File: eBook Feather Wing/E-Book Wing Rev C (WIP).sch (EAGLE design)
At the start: 96 parts, among them IC1 MCP23008/SO, IC2 23K256-I/SN, J1 MJ-3502N, Q1 IRLML0100, SW1 SPDT_SWITCH

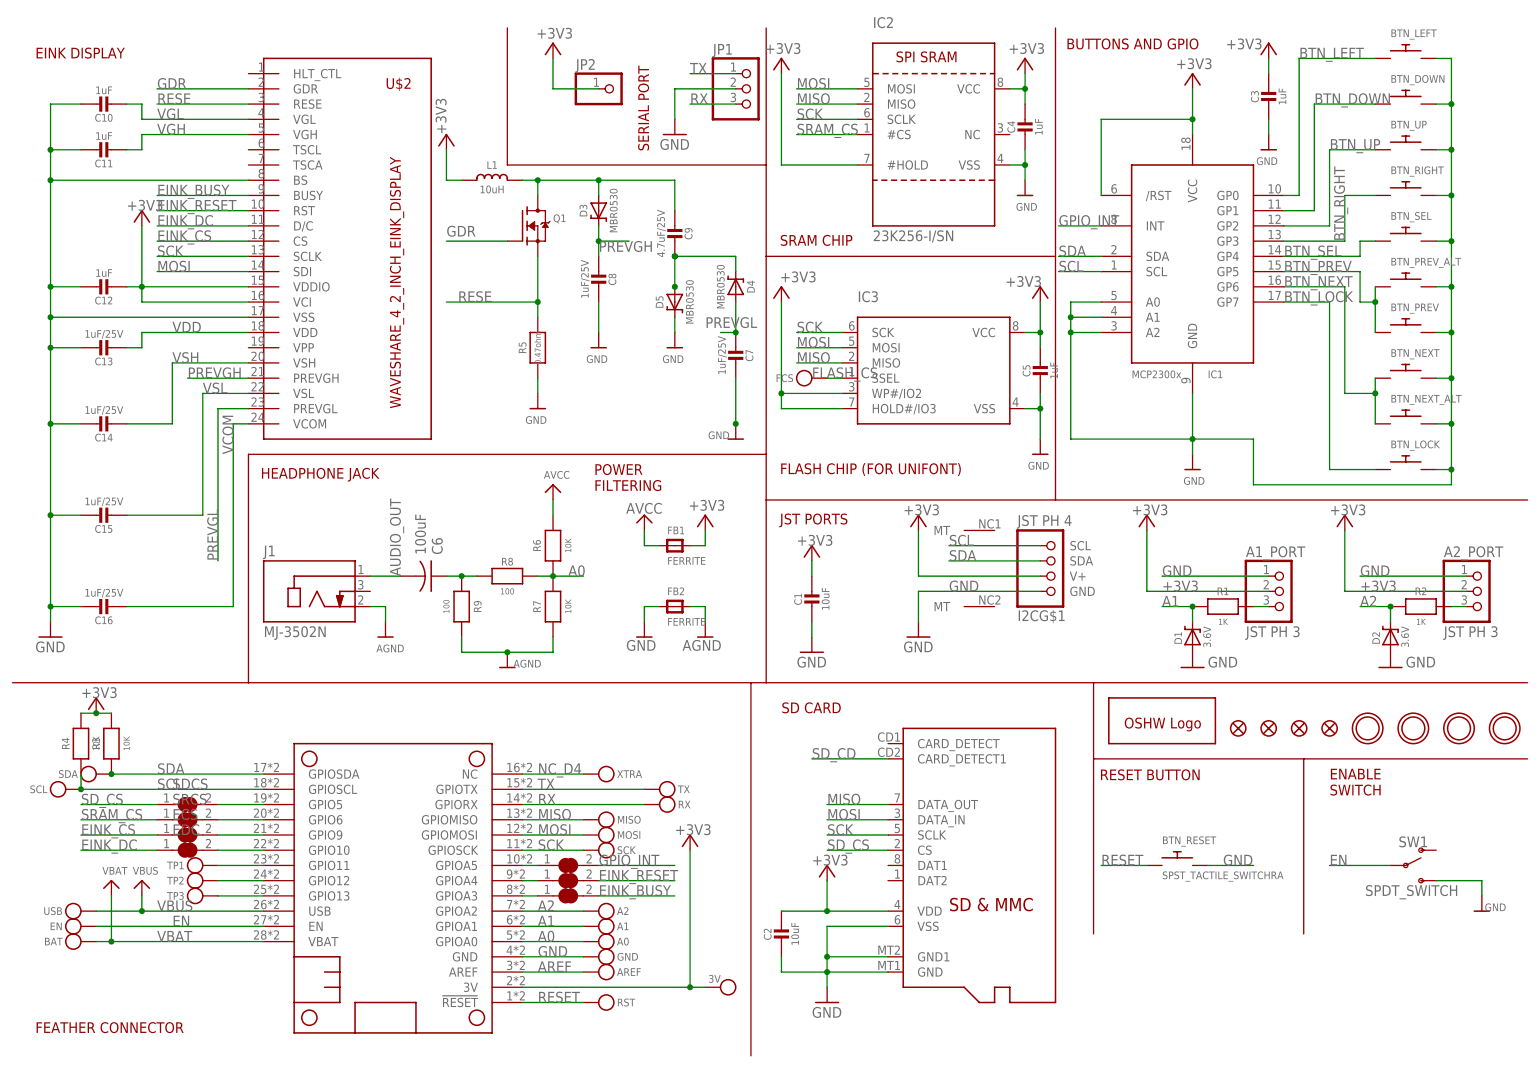
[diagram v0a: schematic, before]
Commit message: surface mount part swap, two more fiducials
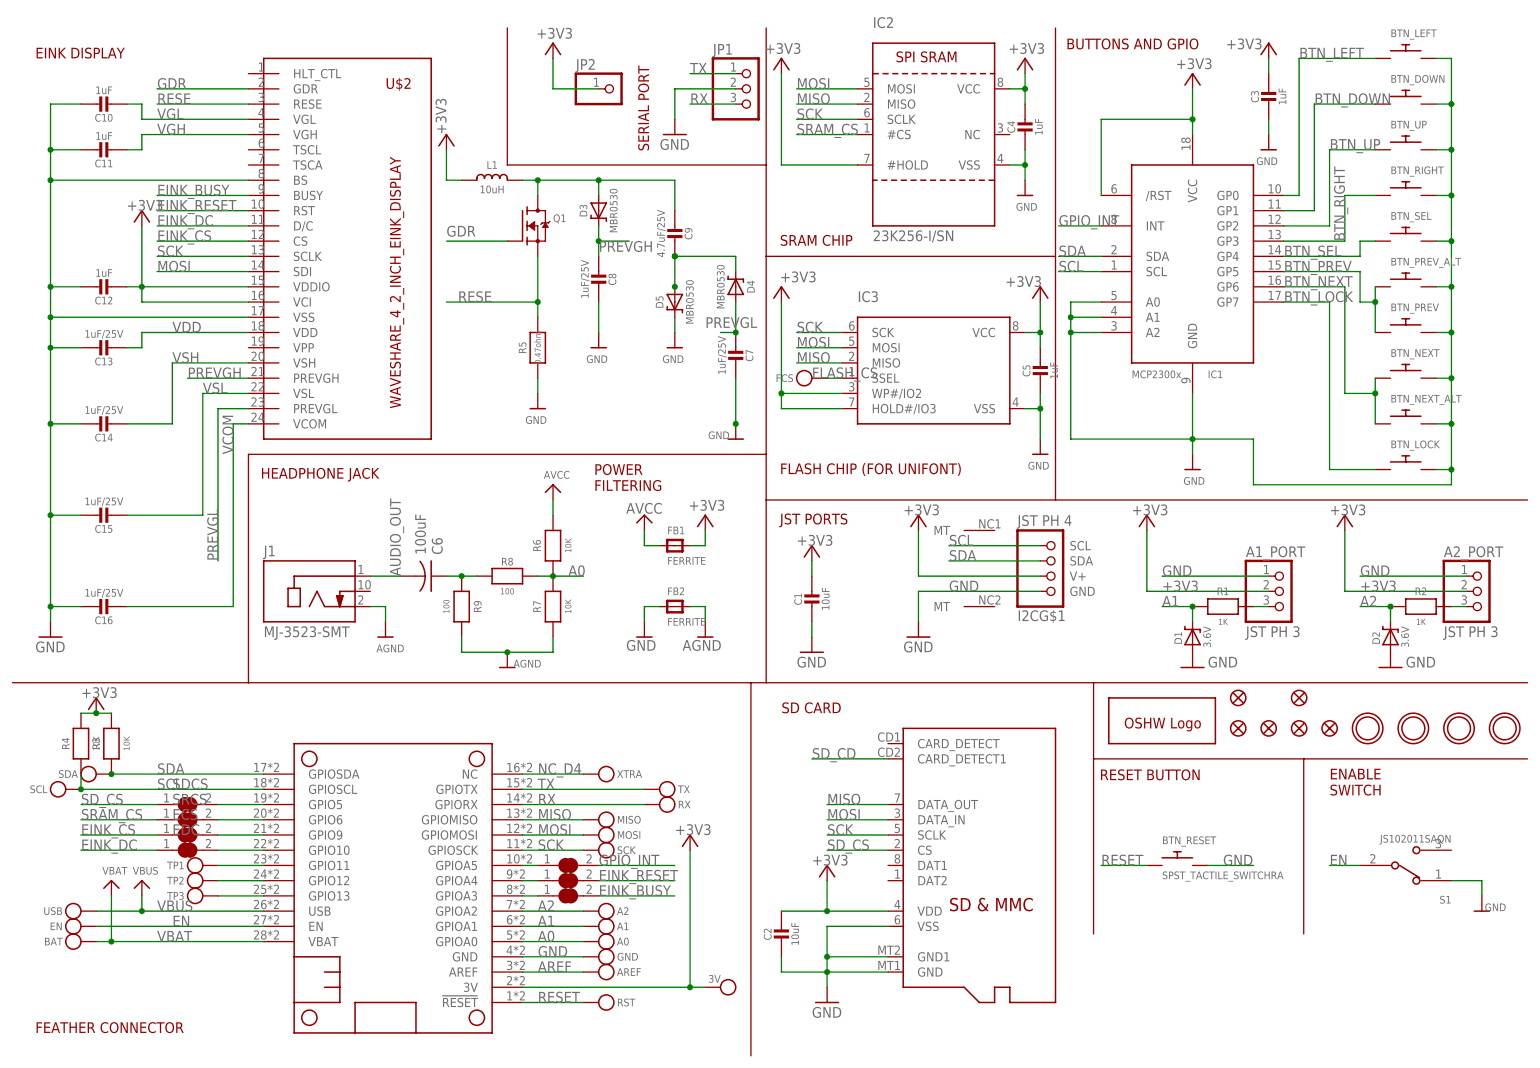
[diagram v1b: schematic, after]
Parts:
- removed SW1: SPDT_SWITCH, My Stuff:SPDT_SWITCH
- added FID5, FID6: FIDUCIAL_1MM, microbuilder:FIDUCIAL_1MM
- added S1: JS102011SAQN, JS102011SAQN:JS102011SAQN
- J1: value MJ-3502N -> MJ-3523-SMT; device MJ-3502N:MJ-3502N -> MJ-3523-SMT:MJ-3523-SMT
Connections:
- net EN: now also S1.2; no longer SW1.P
- net GND: now also S1.1; no longer SW1.S
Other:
- moved on the sheet: J1

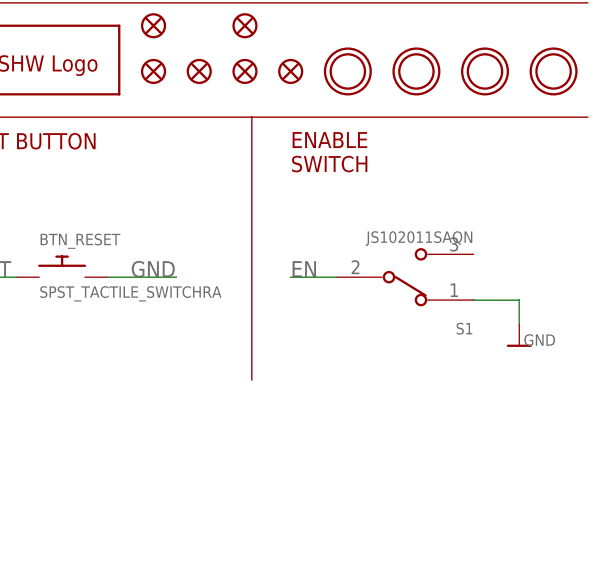
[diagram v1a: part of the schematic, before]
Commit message: lol nevermind this thru-hole switch is cheaper
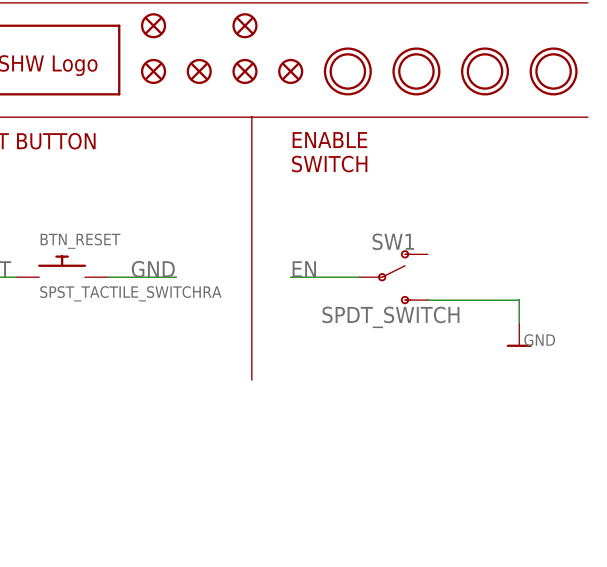
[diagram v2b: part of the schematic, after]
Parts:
- removed S1: JS102011SAQN, JS102011SAQN:JS102011SAQN
- added SW1: SPDT_SWITCH, My Stuff:SPDT_SWITCH
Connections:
- net EN: now also SW1.P; no longer S1.2
- net GND: now also SW1.S; no longer S1.1
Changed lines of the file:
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@@
 <?xml version="1.0" encoding="utf-8"?>
 <!DOCTYPE eagle SYSTEM "eagle.dtd">
-<eagle version="9.3.0">
+<eagle version="9.4.2">
 <drawing>
 <settings>
@@
 <part name="BTN_LOCK" library="My Stuff" deviceset="SPST_TACTILE_SWITCH" device="RA"/>
 <part name="J1" library="MJ-3523-SMT" deviceset="MJ-3523-SMT" device=""/>
-<part name="S1" library="JS102011SAQN" deviceset="JS102011SAQN" device=""/>
 <part name="FID5" library="microbuilder" deviceset="FIDUCIAL" device="_1MM"/>
 <part name="FID6" library="microbuilder" deviceset="FIDUCIAL" device="_1MM"/>
+<part name="SW1" library="My Stuff" deviceset="SPDT_SWITCH" device=""/>
 </parts>
 <sheets>
@@
 <attribute name="VALUE" x="45.708259375" y="73.648259375" size="1.780740625" layer="96"/>
 </instance>
-<instance part="S1" gate="G$1" x="236.22" y="35.56" smashed="yes" rot="R180">
-<attribute name="NAME" x="243.842909375" y="30.478059375" size="1.270490625" layer="95" rot="R180"/>
-<attribute name="VALUE" x="243.848559375" y="40.645709375" size="1.27143125" layer="96" rot="R180"/>
-</instance>
 <instance part="FID5" gate="G$1" x="208.28" y="63.5" smashed="yes"/>
 <instance part="FID6" gate="G$1" x="218.44" y="63.5" smashed="yes"/>
+<instance part="SW1" gate="G$1" x="233.68" y="35.56" smashed="yes">
+<attribute name="NAME" x="234.95" y="38.608" size="1.778" layer="95" font="vector" align="bottom-center"/>
+<attribute name="VALUE" x="234.696" y="32.258" size="1.778" layer="96" font="vector" align="top-center"/>
+</instance>
 </instances>
 <busses>
@@
 <segment>
 <pinref part="U$12" gate="G$1" pin="GND"/>
-<wire x1="243.84" y1="33.02" x2="248.92" y2="33.02" width="0.1524" layer="91"/>
+<wire x1="238.76" y1="33.02" x2="248.92" y2="33.02" width="0.1524" layer="91"/>
 <wire x1="248.92" y1="33.02" x2="248.92" y2="30.48" width="0.1524" layer="91"/>
-<pinref part="S1" gate="G$1" pin="1"/>
+<pinref part="SW1" gate="G$1" pin="S"/>
 </segment>
 <segment>
@@
 <segment>
 <label x="223.52" y="35.56" size="1.778" layer="95"/>
-<pinref part="S1" gate="G$1" pin="2"/>
-<wire x1="228.6" y1="35.56" x2="223.52" y2="35.56" width="0.1524" layer="91"/>
-</segment>
-</net>
+<wire x1="231.14" y1="35.56" x2="223.52" y2="35.56" width="0.1524" layer="91"/>
+<pinref part="SW1" gate="G$1" pin="P"/>
+</segment>
+</net>

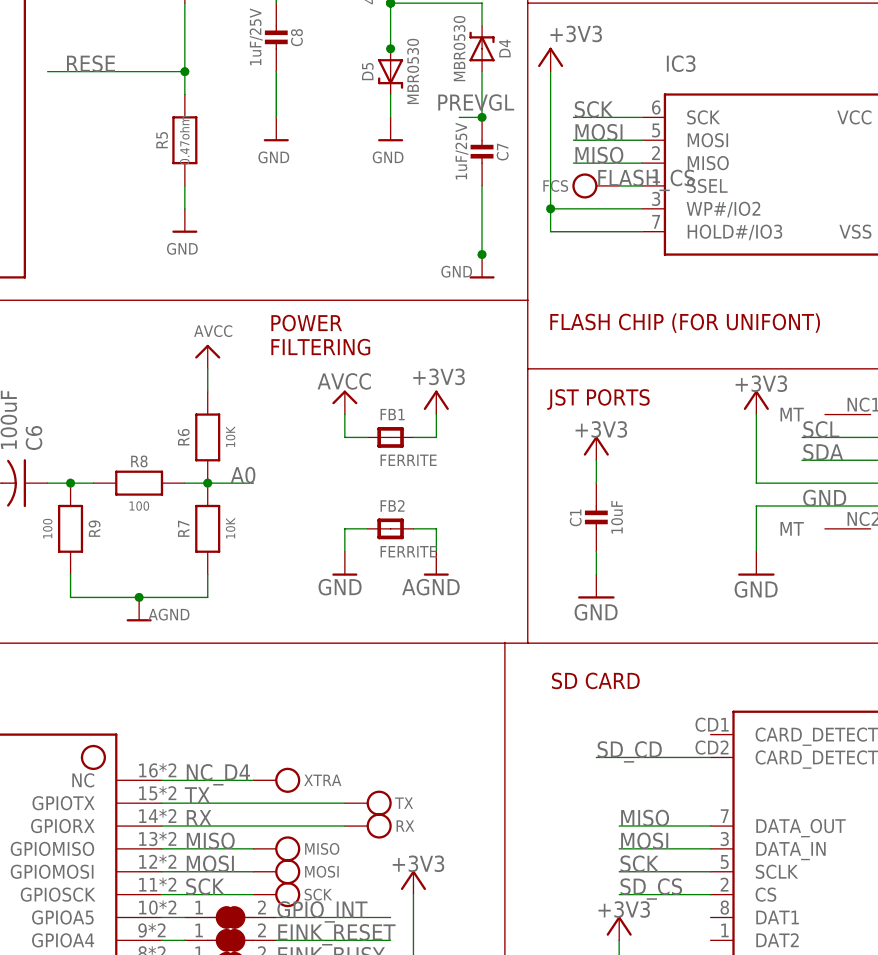
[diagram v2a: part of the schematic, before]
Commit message: wire FCS to M4's 'extra' pin
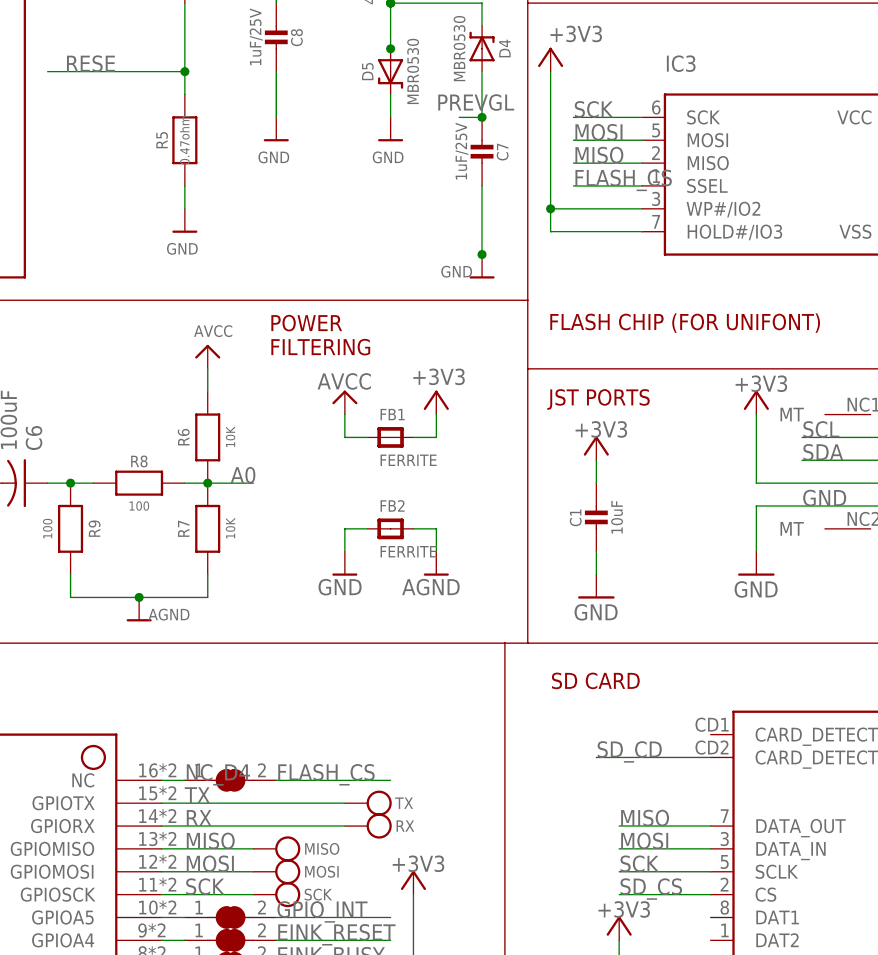
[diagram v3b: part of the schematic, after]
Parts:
- removed XTRA: (no value), Adafruit 3.5in 480x320 FeatherWing:MICROBUILDER_TESTPOINT1.5X2.0MM_NOCREAM
- FCS: device Adafruit 3.5in 480x320 FeatherWing:MICROBUILDER_TESTPOINTPAD1MM -> Adafruit 3.5in 480x320 FeatherWing:MICROBUILDER_SOLDERJUMPER_CLOSED
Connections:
- net FLASH_CS: now also FCS.2; no longer FCS.P$1
- net NC_D4: now also FCS.1; no longer XTRA.P$1
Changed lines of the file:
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@@
 <part name="RX" library="Adafruit 3.5in 480x320 FeatherWing" deviceset="MICROBUILDER_TESTPOINT" device="1.5X2.0MM_NOCREAM"/>
 <part name="TX" library="Adafruit 3.5in 480x320 FeatherWing" deviceset="MICROBUILDER_TESTPOINT" device="1.5X2.0MM_NOCREAM"/>
-<part name="XTRA" library="Adafruit 3.5in 480x320 FeatherWing" deviceset="MICROBUILDER_TESTPOINT" device="1.5X2.0MM_NOCREAM"/>
 <part name="+3V7" library="supply1" library_urn="urn:adsk.eagle:library:371" deviceset="+3V3" device=""/>
 <part name="+3V8" library="supply1" library_urn="urn:adsk.eagle:library:371" deviceset="+3V3" device=""/>
@@
 <part name="ERST" library="Adafruit 3.5in 480x320 FeatherWing" deviceset="MICROBUILDER_SOLDERJUMPER_CLOSED" device=""/>
 <part name="EBSY" library="Adafruit 3.5in 480x320 FeatherWing" deviceset="MICROBUILDER_SOLDERJUMPER_CLOSED" device=""/>
-<part name="FCS" library="Adafruit 3.5in 480x320 FeatherWing" deviceset="MICROBUILDER_TESTPOINT" device="PAD1MM"/>
 <part name="BTN_RIGHT" library="My Stuff" deviceset="MJTP1250_SPST_SWITCH" device=""/>
 <part name="BTN_LEFT" library="My Stuff" deviceset="MJTP1250_SPST_SWITCH" device=""/>
@@
 <part name="FID6" library="microbuilder" deviceset="FIDUCIAL" device="_1MM"/>
 <part name="SW1" library="My Stuff" deviceset="SPDT_SWITCH" device=""/>
+<part name="FCS" library="Adafruit 3.5in 480x320 FeatherWing" deviceset="MICROBUILDER_SOLDERJUMPER_CLOSED" device=""/>
 </parts>
 <sheets>
@@
 <attribute name="VALUE" x="114.808" y="46.609" size="1.27" layer="95" align="center-left"/>
 </instance>
-<instance part="XTRA" gate="G$1" x="99.06" y="50.8" smashed="yes" rot="R270">
-<attribute name="NAME" x="104.648" y="50.8" size="1.27" layer="95" align="center-left"/>
-<attribute name="VALUE" x="104.648" y="49.149" size="1.27" layer="95" align="center-left"/>
-</instance>
 <instance part="+3V7" gate="G$1" x="76.2" y="157.48" smashed="yes">
 <attribute name="VALUE" x="76.2" y="157.48" size="1.778" layer="96" rot="R90"/>
@@
 <instance part="EBSY" gate="G$1" x="96.52" y="30.48" smashed="yes">
 <attribute name="VALUE" x="93.98" y="26.67" size="1.778" layer="96"/>
-</instance>
-<instance part="FCS" gate="G$1" x="139.7" y="116.84" smashed="yes" rot="R90">
-<attribute name="NAME" x="134.112" y="116.84" size="1.27" layer="95" rot="R180" align="center-left"/>
-<attribute name="VALUE" x="134.112" y="118.491" size="1.27" layer="95" rot="R180" align="center-left"/>
 </instance>
 <instance part="BTN_RIGHT" gate="G$1" x="236.22" y="147.32" smashed="yes">
@@
 <attribute name="NAME" x="234.95" y="38.608" size="1.778" layer="95" font="vector" align="bottom-center"/>
 <attribute name="VALUE" x="234.696" y="32.258" size="1.778" layer="96" font="vector" align="top-center"/>
+</instance>
+<instance part="FCS" gate="G$1" x="96.52" y="50.8" smashed="yes">
+<attribute name="VALUE" x="93.98" y="46.99" size="1.778" layer="96"/>
 </instance>
 </instances>
@@
 <segment>
 <pinref part="MS1" gate="G$1" pin="NC"/>
-<wire x1="88.9" y1="50.8" x2="99.06" y2="50.8" width="0.1524" layer="91"/>
+<wire x1="88.9" y1="50.8" x2="91.44" y2="50.8" width="0.1524" layer="91"/>
 <label x="91.44" y="50.8" size="1.778" layer="95"/>
-<pinref part="XTRA" gate="G$1" pin="P$1"/>
+<pinref part="FCS" gate="G$1" pin="1"/>
 </segment>
 </net>
@@
 <segment>
 <pinref part="IC3" gate="G$1" pin="SSEL"/>
-<wire x1="142.24" y1="116.84" x2="139.7" y2="116.84" width="0.1524" layer="91"/>
-<label x="137.16" y="116.84" size="1.778" layer="95"/>
-<pinref part="FCS" gate="G$1" pin="P$1"/>
-</segment>
-</net>
+<wire x1="142.24" y1="116.84" x2="134.62" y2="116.84" width="0.1524" layer="91"/>
+<label x="134.62" y="116.84" size="1.778" layer="95"/>
+</segment>
+<segment>
+<pinref part="FCS" gate="G$1" pin="2"/>
+<wire x1="101.6" y1="50.8" x2="114.3" y2="50.8" width="0.1524" layer="91"/>
+<label x="101.6" y="50.8" size="1.778" layer="95"/>
+</segment>
+</net>

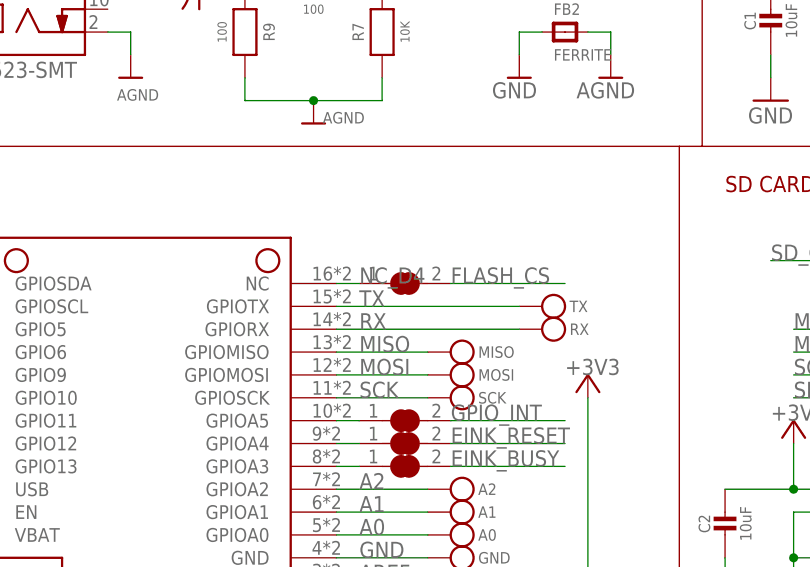
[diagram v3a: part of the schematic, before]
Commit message: make the FCS jumper open by default
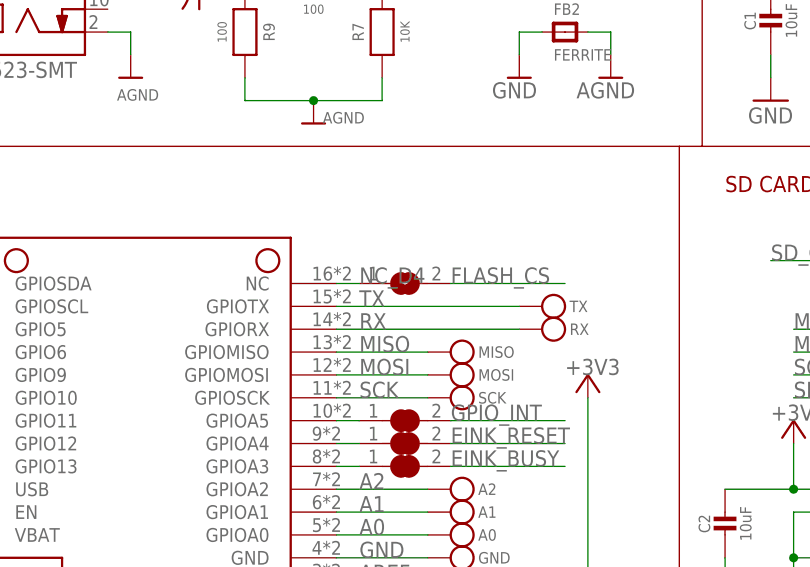
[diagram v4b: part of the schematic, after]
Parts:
- FCS: value (none) -> SOLDERJUMPER_OPEN; device Adafruit 3.5in 480x320 FeatherWing:MICROBUILDER_SOLDERJUMPER_CLOSED -> E-Book Wing Rev C (WIP):SOLDERJUMPER_OPEN
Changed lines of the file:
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@@
 <part name="FID6" library="microbuilder" deviceset="FIDUCIAL" device="_1MM"/>
 <part name="SW1" library="My Stuff" deviceset="SPDT_SWITCH" device=""/>
-<part name="FCS" library="Adafruit 3.5in 480x320 FeatherWing" deviceset="MICROBUILDER_SOLDERJUMPER_CLOSED" device=""/>
+<part name="FCS" library="E-Book Wing Rev C (WIP)" deviceset="SOLDERJUMPER_OPEN" device=""/>
 </parts>
 <sheets>
@@
 <attribute name="VALUE" x="234.696" y="32.258" size="1.778" layer="96" font="vector" align="top-center"/>
 </instance>
-<instance part="FCS" gate="G$1" x="96.52" y="50.8" smashed="yes">
-<attribute name="VALUE" x="93.98" y="46.99" size="1.778" layer="96"/>
-</instance>
+<instance part="FCS" gate="G$1" x="96.52" y="50.8" smashed="yes"/>
 </instances>
 <busses>
@@
 </segment>
 <segment>
-<pinref part="FCS" gate="G$1" pin="2"/>
 <wire x1="101.6" y1="50.8" x2="114.3" y2="50.8" width="0.1524" layer="91"/>
 <label x="101.6" y="50.8" size="1.778" layer="95"/>
-</segment>
-</net>
+<pinref part="FCS" gate="G$1" pin="2"/>
+</segment>
+</net>
